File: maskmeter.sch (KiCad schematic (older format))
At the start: 12 parts, among them SW1 SW_Push, U1 TLC555IDR

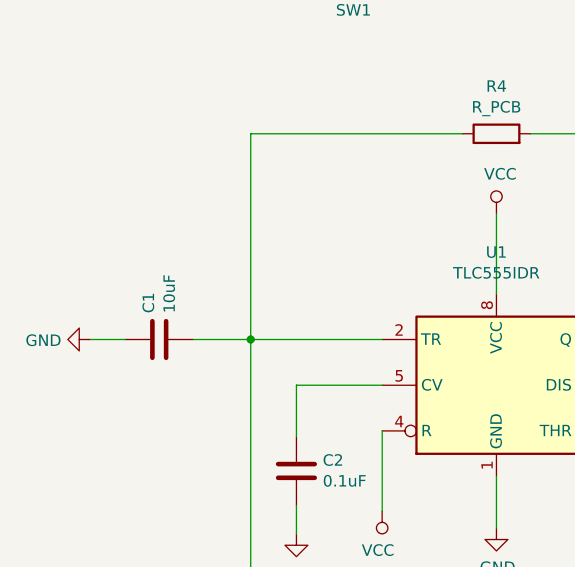
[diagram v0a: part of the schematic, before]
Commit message: Updated battery holder
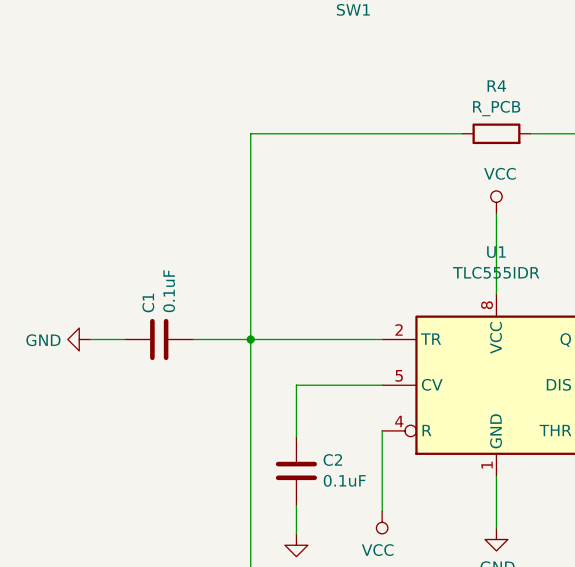
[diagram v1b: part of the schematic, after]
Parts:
- BT1: footprint maskmeter:QJ.BS-6 -> Battery:BatteryHolder_Keystone_1060_1x2032
- C1: value 10uF -> 0.1uF; LCSC C19702 -> C14663
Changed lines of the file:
@@
 F 0 "BT1" H 5068 1996 50  0000 L CNN
 F 1 "Battery_Cell" H 5068 1905 50  0000 L CNN
-F 2 "maskmeter:QJ.BS-6" V 4950 1960 50  0001 C CNN
+F 2 "Battery:BatteryHolder_Keystone_1060_1x2032" V 4950 1960 50  0001 C CNN
 F 3 "~" V 4950 1960 50  0001 C CNN
 F 4 "C70377" H 4950 1900 50  0001 C CNN "LCSC"
@@
 P 3500 3625
 F 0 "C1" H 3615 3671 50  0000 L CNN
-F 1 "10uF" H 3615 3580 50  0000 L CNN
+F 1 "0.1uF" H 3615 3580 50  0000 L CNN
 F 2 "Capacitor_SMD:C_0603_1608Metric" H 3538 3475 50  0001 C CNN
 F 3 "~" H 3500 3625 50  0001 C CNN
-F 4 "C19702" H 3500 3625 50  0001 C CNN "LCSC"
+F 4 "C14663" H 3500 3625 50  0001 C CNN "LCSC"
 	1    3500 3625
 	0    -1   -1   0
